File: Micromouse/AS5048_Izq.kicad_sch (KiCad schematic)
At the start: 6 parts, among them J9 AS5048_Izq, U3 AS5048B-HTSP

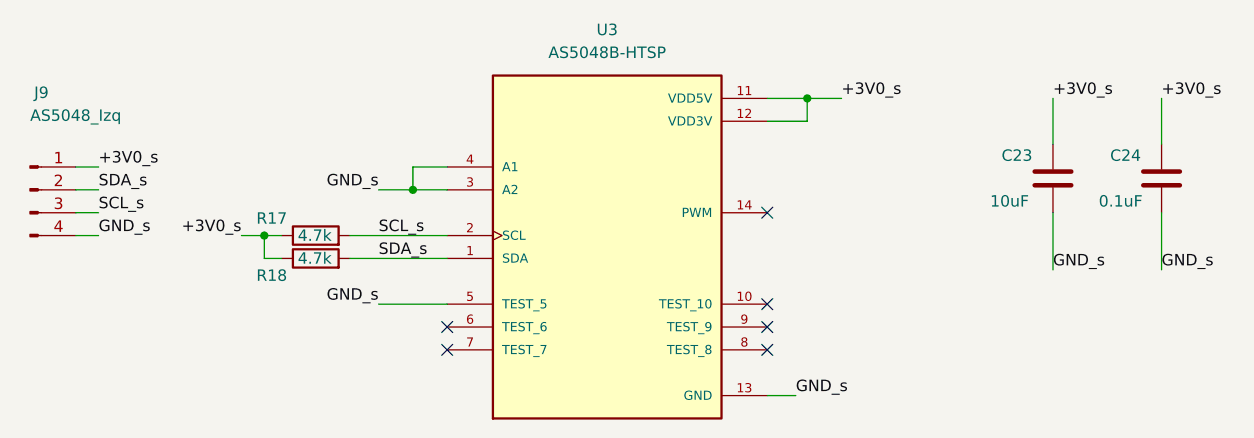
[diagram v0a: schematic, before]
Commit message: Añadiendo el chasis de minisumo
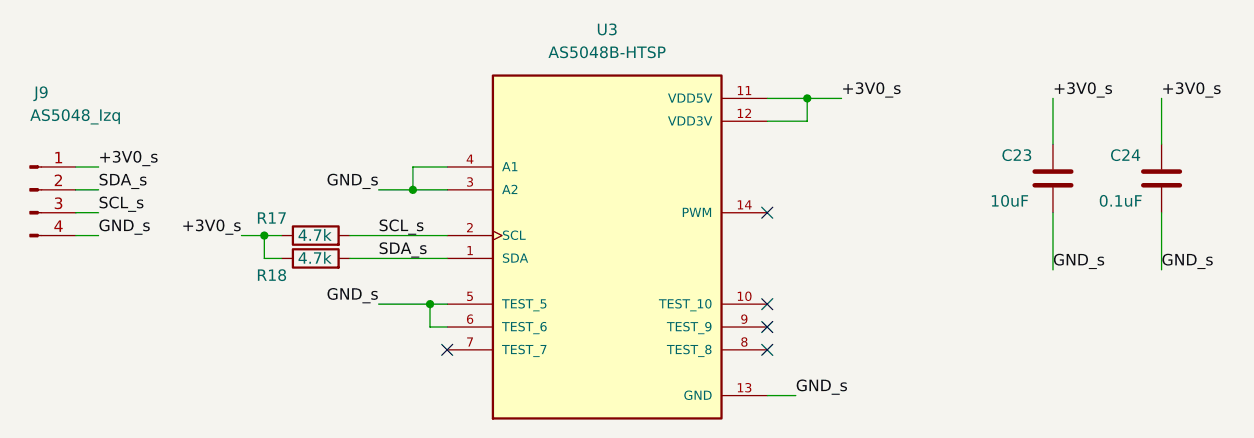
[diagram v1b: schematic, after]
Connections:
- net GND_s: now also U3.6 (TEST_6)
- no-connect marks 6 -> 5
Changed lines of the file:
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@@
+	)
+	(junction
+		(at 131.445 113.03)
+		(diameter 0)
+		(color 0 0 0 0)
 	)
 	(junction
@@
 	)
 	(no_connect
-		(at 133.35 115.57)
-	)
-	(no_connect
 		(at 168.91 102.87)
 	)
@@
 	(wire
 		(pts
-			(xy 125.73 113.03) (xy 133.35 113.03)
+			(xy 131.445 113.03) (xy 133.35 113.03)
+		)
+		(stroke
+			(width 0)
+			(type default)
+		)
+	)
+	(wire
+		(pts
+			(xy 125.73 113.03) (xy 131.445 113.03)
 		)
 		(stroke
@@
 	(wire
 		(pts
+			(xy 133.35 115.57) (xy 131.445 115.57)
+		)
+		(stroke
+			(width 0)
+			(type default)
+		)
+	)
+	(wire
+		(pts
 			(xy 168.91 90.17) (xy 173.355 90.17)
 		)
@@
 		)
 		(stroke
+			(width 0)
+			(type default)
+		)
+	)
+	(wire
+		(pts
+			(xy 131.445 115.57) (xy 131.445 113.03)
+		)
+		(stroke

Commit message: Commit4
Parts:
- renumbered C23 to C45, C24 to C46, R17 to R31, R18 to R32
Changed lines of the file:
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@@
 		(on_board yes)
 		(dnp no)
-		(property "Reference" "R17"
+		(property "Reference" "R31"
 			(at 115.57 103.505 90)
 			(effects
@@
 			(project "Half-Size Micromouse"
 				(path "/96b72c82-8e98-4b00-820e-849de0fa96c7/30dace89-d7fa-480e-aff2-f8c5b12c4053"
-					(reference "R17")
+					(reference "R31")
 					(unit 1)
 				)
@@
 		(on_board yes)
 		(dnp no)
-		(property "Reference" "C24"
+		(property "Reference" "C46"
 			(at 207.01 96.52 0)
 			(effects
@@
 			(project "Half-Size Micromouse"
 				(path "/96b72c82-8e98-4b00-820e-849de0fa96c7/30dace89-d7fa-480e-aff2-f8c5b12c4053"
-					(reference "C24")
+					(reference "C46")
 					(unit 1)
 				)
@@
 		(on_board yes)
 		(dnp no)
-		(property "Reference" "R18"
+		(property "Reference" "R32"
 			(at 115.57 109.855 90)
 			(effects
@@
 			(project "Half-Size Micromouse"
 				(path "/96b72c82-8e98-4b00-820e-849de0fa96c7/30dace89-d7fa-480e-aff2-f8c5b12c4053"
-					(reference "R18")
+					(reference "R32")
 					(unit 1)
 				)
@@
 		(on_board yes)
 		(dnp no)
-		(property "Reference" "C23"
+		(property "Reference" "C45"
 			(at 194.945 96.52 0)
 			(effects
@@
 			(project "Half-Size Micromouse"
 				(path "/96b72c82-8e98-4b00-820e-849de0fa96c7/30dace89-d7fa-480e-aff2-f8c5b12c4053"
-					(reference "C23")
+					(reference "C45")
 					(unit 1)
 				)

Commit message: Chasis minisumo terminado
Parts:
- C43: renamed from C45; footprint Capacitor_SMD:C_0805_2012Metric -> Capacitor_SMD:C_0402_1005Metric
- C44: renamed from C46; footprint Capacitor_SMD:C_0201_0603Metric -> Capacitor_SMD:C_0402_1005Metric
- R31, R32: footprint Resistor_SMD:R_0201_0603Metric -> Resistor_SMD:R_0402_1005Metric
- renumbered J9 to J10, U3 to U4
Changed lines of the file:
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@@
 		(dnp no)
 		(fields_autoplaced yes)
-		(property "Reference" "U3"
+		(property "Reference" "U4"
 			(at 151.13 82.55 0)
 			(effects
@@
 		)
 		(property "VACANCIES" ""
+			(at 151.13 105.41 0)
+			(effects
+				(font
+					(size 1.27 1.27)
+				)
+				(hide yes)
+			)
+		)
+		(property "CREATOR" ""
+			(at 151.13 105.41 0)
+			(effects
+				(font
+					(size 1.27 1.27)
+				)
+				(hide yes)
+			)
+		)
+		(property "Sim.Pins" ""
+			(at 151.13 105.41 0)
+			(effects
+				(font
+					(size 1.27 1.27)
+				)
+				(hide yes)
+			)
+		)
+		(property "VERIFIER" ""
 			(at 151.13 105.41 0)
 			(effects
@@
 			(project ""
 				(path "/96b72c82-8e98-4b00-820e-849de0fa96c7/30dace89-d7fa-480e-aff2-f8c5b12c4053"
-					(reference "U3")
+					(reference "U4")
 					(unit 1)
 				)
@@
 			)
 		)
-		(property "Footprint" "Resistor_SMD:R_0201_0603Metric"
+		(property "Footprint" "Resistor_SMD:R_0402_1005Metric"
 			(at 118.745 107.188 90)
 			(effects
@@
 		)
 		(property "VACANCIES" ""
+			(at 118.745 105.41 90)
+			(effects
+				(font
+					(size 1.27 1.27)
+				)
+				(hide yes)
+			)
+		)
+		(property "CREATOR" ""
+			(at 118.745 105.41 90)
+			(effects
+				(font
+					(size 1.27 1.27)
+				)
+				(hide yes)
+			)
+		)
+		(property "Sim.Pins" ""
+			(at 118.745 105.41 90)
+			(effects
+				(font
+					(size 1.27 1.27)
+				)
+				(hide yes)
+			)
+		)
+		(property "VERIFIER" ""
 			(at 118.745 105.41 90)
 			(effects
@@
 		(on_board yes)
 		(dnp no)
-		(property "Reference" "J9"
+		(property "Reference" "J10"
 			(at 88.265 89.535 0)
 			(effects
@@
 		)
 		(property "VACANCIES" ""
+			(at 86.995 100.33 0)
+			(effects
+				(font
+					(size 1.27 1.27)
+				)
+				(hide yes)
+			)
+		)
+		(property "CREATOR" ""
+			(at 86.995 100.33 0)
+			(effects
+				(font
+					(size 1.27 1.27)
+				)
+				(hide yes)
+			)
+		)
+		(property "Sim.Pins" ""
+			(at 86.995 100.33 0)
+			(effects
+				(font
+					(size 1.27 1.27)
+				)
+				(hide yes)
+			)
+		)
+		(property "VERIFIER" ""
 			(at 86.995 100.33 0)
 			(effects
@@
 			(project "Half-Size Micromouse"
 				(path "/96b72c82-8e98-4b00-820e-849de0fa96c7/30dace89-d7fa-480e-aff2-f8c5b12c4053"
-					(reference "J9")
+					(reference "J10")
 					(unit 1)
 				)
@@
 		(on_board yes)
 		(dnp no)
-		(property "Reference" "C46"
+		(property "Reference" "C44"
 			(at 207.01 96.52 0)
 			(effects
@@
 			)
 		)
-		(property "Footprint" "Capacitor_SMD:C_0201_0603Metric"
+		(property "Footprint" "Capacitor_SMD:C_0402_1005Metric"
 			(at 213.6902 102.87 0)
 			(effects
@@
 		)
 		(property "VACANCIES" ""
+			(at 212.725 99.06 0)
+			(effects
+				(font
+					(size 1.27 1.27)
+				)
+				(hide yes)
+			)
+		)
+		(property "CREATOR" ""
+			(at 212.725 99.06 0)
+			(effects
+				(font
+					(size 1.27 1.27)
+				)
+				(hide yes)
+			)
+		)
+		(property "Sim.Pins" ""
+			(at 212.725 99.06 0)
+			(effects
+				(font
+					(size 1.27 1.27)
+				)
+				(hide yes)
+			)
+		)
+		(property "VERIFIER" ""
 			(at 212.725 99.06 0)
 			(effects
@@
 			(project "Half-Size Micromouse"
 				(path "/96b72c82-8e98-4b00-820e-849de0fa96c7/30dace89-d7fa-480e-aff2-f8c5b12c4053"
-					(reference "C46")
+					(reference "C44")
 					(unit 1)
 				)
@@
 			)
 		)
-		(property "Footprint" "Resistor_SMD:R_0201_0603Metric"
+		(property "Footprint" "Resistor_SMD:R_0402_1005Metric"
 			(at 118.745 109.728 90)
 			(effects
@@
 		)
 		(property "VACANCIES" ""
+			(at 118.745 107.95 90)
+			(effects
+				(font
+					(size 1.27 1.27)
+				)
+				(hide yes)
+			)
+		)
+		(property "CREATOR" ""
+			(at 118.745 107.95 90)
+			(effects
+				(font
+					(size 1.27 1.27)
+				)
+				(hide yes)
+			)
+		)
+		(property "Sim.Pins" ""
+			(at 118.745 107.95 90)
+			(effects
+				(font
+					(size 1.27 1.27)
+				)
+				(hide yes)
+			)
+		)
+		(property "VERIFIER" ""
 			(at 118.745 107.95 90)
 			(effects
@@
 		(on_board yes)
 		(dnp no)
-		(property "Reference" "C45"
+		(property "Reference" "C43"
 			(at 194.945 96.52 0)
 			(effects
@@
 			)
 		)
-		(property "Footprint" "Capacitor_SMD:C_0805_2012Metric"
+		(property "Footprint" "Capacitor_SMD:C_0402_1005Metric"
 			(at 201.6252 102.87 0)
 			(effects
@@
 		)
 		(property "VACANCIES" ""
+			(at 200.66 99.06 0)
+			(effects
+				(font
+					(size 1.27 1.27)
+				)
+				(hide yes)
+			)
+		)
+		(property "CREATOR" ""
+			(at 200.66 99.06 0)
+			(effects
+				(font
+					(size 1.27 1.27)
+				)
+				(hide yes)
+			)
+		)
+		(property "Sim.Pins" ""
+			(at 200.66 99.06 0)
+			(effects
+				(font
+					(size 1.27 1.27)
+				)
+				(hide yes)
+			)
+		)
+		(property "VERIFIER" ""
 			(at 200.66 99.06 0)
 			(effects
@@
 			(project "Half-Size Micromouse"
 				(path "/96b72c82-8e98-4b00-820e-849de0fa96c7/30dace89-d7fa-480e-aff2-f8c5b12c4053"
-					(reference "C45")
+					(reference "C43")
 					(unit 1)
 				)
